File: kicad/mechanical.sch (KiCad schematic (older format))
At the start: 70 parts, among them J1 CLK_IN, J10 DAT_IN, J15 5V, J16 GND, J2 DAT_IN, J7 5V, J8 GND, J9 CLK_IN

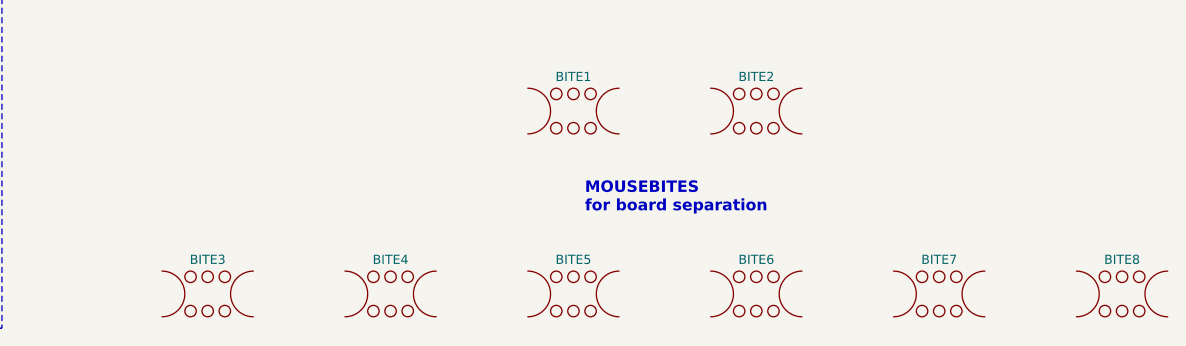
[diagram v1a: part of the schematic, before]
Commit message: KiCad v5 - new expansion headers, new qwiic headers, wider breakoff tabs
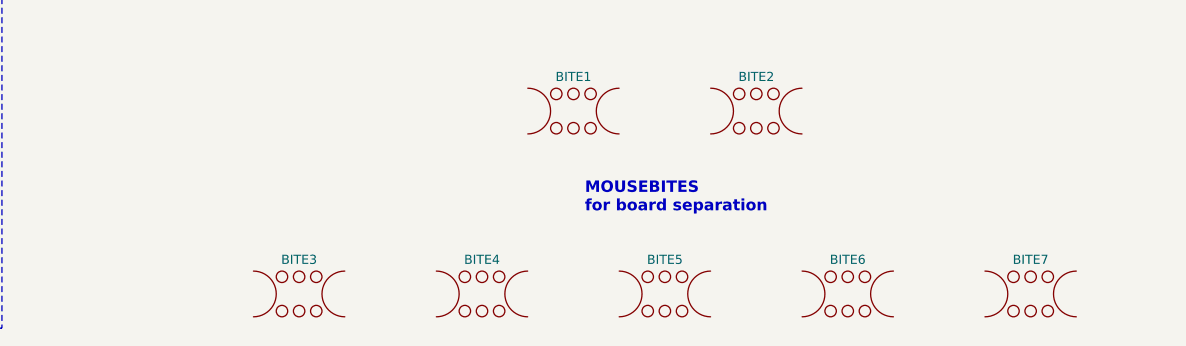
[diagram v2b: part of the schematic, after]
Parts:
- removed BITE8: Mouse_Bite, ClockIOT_libs:mouse-bite-2.54mm-slot_OSH, symbol ClockIOT:Mouse_Bite
- BITE1, BITE2, BITE3, BITE4, BITE5, BITE6, BITE7: footprint ClockIOT_libs:mouse-bite-2.54mm-slot_OSH -> ClockIOT_libs:mouse-bite-0.3in-slot_OSH
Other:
- moved on the sheet: BITE3, BITE4, BITE5, BITE6, BITE7
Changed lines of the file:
@@
 EESchema Schematic File Version 4
-LIBS:ClockIOT-cache
-EELAYER 26 0
+EELAYER 30 0
 EELAYER END
 $Descr A4 11693 8268
@@
 F 0 "BITE1" H 8100 5050 40  0000 C CNN
 F 1 "Mouse_Bite" H 8100 5025 30  0001 C CNN
-F 2 "ClockIOT_libs:mouse-bite-2.54mm-slot_OSH" H 8100 4900 60  0001 C CNN
+F 2 "ClockIOT_libs:mouse-bite-0.3in-slot_OSH" H 8100 4900 60  0001 C CNN
 F 3 "" H 8100 4900 60  0000 C CNN
 F 4 "mfr_pn" H 8100 4900 50  0001 C CNN "manf#"
@@
 F 0 "BITE2" H 8900 5050 40  0000 C CNN
 F 1 "Mouse_Bite" H 8900 5025 30  0001 C CNN
-F 2 "ClockIOT_libs:mouse-bite-2.54mm-slot_OSH" H 8900 4900 60  0001 C CNN
+F 2 "ClockIOT_libs:mouse-bite-0.3in-slot_OSH" H 8900 4900 60  0001 C CNN
 F 3 "" H 8900 4900 60  0000 C CNN
 F 4 "mfr_pn" H 8900 4900 50  0001 C CNN "manf#"
@@
 L ClockIOT:Mouse_Bite BITE5
 U 1 1 5A4A2BA0
-P 8100 5700
-F 0 "BITE5" H 8100 5850 40  0000 C CNN
-F 1 "Mouse_Bite" H 8100 5825 30  0001 C CNN
-F 2 "ClockIOT_libs:mouse-bite-2.54mm-slot_OSH" H 8100 5700 60  0001 C CNN
-F 3 "" H 8100 5700 60  0000 C CNN
-F 4 "mfr_pn" H 8100 5700 50  0001 C CNN "manf#"
-	1    8100 5700
+P 8500 5700
+F 0 "BITE5" H 8500 5850 40  0000 C CNN
+F 1 "Mouse_Bite" H 8500 5825 30  0001 C CNN
+F 2 "ClockIOT_libs:mouse-bite-0.3in-slot_OSH" H 8500 5700 60  0001 C CNN
+F 3 "" H 8500 5700 60  0000 C CNN
+F 4 "mfr_pn" H 8500 5700 50  0001 C CNN "manf#"
+	1    8500 5700
 	1    0    0    -1
 $EndComp
@@
 L ClockIOT:Mouse_Bite BITE6
 U 1 1 5A4A2BA6
-P 8900 5700
-F 0 "BITE6" H 8900 5850 40  0000 C CNN
-F 1 "Mouse_Bite" H 8900 5825 30  0001 C CNN
-F 2 "ClockIOT_libs:mouse-bite-2.54mm-slot_OSH" H 8900 5700 60  0001 C CNN
-F 3 "" H 8900 5700 60  0000 C CNN
-F 4 "mfr_pn" H 8900 5700 50  0001 C CNN "manf#"
-	1    8900 5700
+P 9300 5700
+F 0 "BITE6" H 9300 5850 40  0000 C CNN
+F 1 "Mouse_Bite" H 9300 5825 30  0001 C CNN
+F 2 "ClockIOT_libs:mouse-bite-0.3in-slot_OSH" H 9300 5700 60  0001 C CNN
+F 3 "" H 9300 5700 60  0000 C CNN
+F 4 "mfr_pn" H 9300 5700 50  0001 C CNN "manf#"
+	1    9300 5700
 	1    0    0    -1
 $EndComp
@@
 L ClockIOT:Mouse_Bite BITE7
 U 1 1 5A4A2F4F
-P 9700 5700
-F 0 "BITE7" H 9700 5850 40  0000 C CNN
-F 1 "Mouse_Bite" H 9700 5825 30  0001 C CNN
-F 2 "ClockIOT_libs:mouse-bite-2.54mm-slot_OSH" H 9700 5700 60  0001 C CNN
-F 3 "" H 9700 5700 60  0000 C CNN
-F 4 "mfr_pn" H 9700 5700 50  0001 C CNN "manf#"
-	1    9700 5700
-	1    0    0    -1
-$EndComp
-$Comp
-L ClockIOT:Mouse_Bite BITE8
-U 1 1 5A4A2F55
-P 10500 5700
-F 0 "BITE8" H 10500 5850 40  0000 C CNN
-F 1 "Mouse_Bite" H 10500 5825 30  0001 C CNN
-F 2 "ClockIOT_libs:mouse-bite-2.54mm-slot_OSH" H 10500 5700 60  0001 C CNN
-F 3 "" H 10500 5700 60  0000 C CNN
-F 4 "mfr_pn" H 10500 5700 50  0001 C CNN "manf#"
-	1    10500 5700
+P 10100 5700
+F 0 "BITE7" H 10100 5850 40  0000 C CNN
+F 1 "Mouse_Bite" H 10100 5825 30  0001 C CNN
+F 2 "ClockIOT_libs:mouse-bite-0.3in-slot_OSH" H 10100 5700 60  0001 C CNN
+F 3 "" H 10100 5700 60  0000 C CNN
+F 4 "mfr_pn" H 10100 5700 50  0001 C CNN "manf#"
+	1    10100 5700
 	1    0    0    -1
 $EndComp
@@
 L ClockIOT:Mouse_Bite BITE3
 U 1 1 5A4A335C
-P 6500 5700
-F 0 "BITE3" H 6500 5850 40  0000 C CNN
-F 1 "Mouse_Bite" H 6500 5825 30  0001 C CNN
-F 2 "ClockIOT_libs:mouse-bite-2.54mm-slot_OSH" H 6500 5700 60  0001 C CNN
-F 3 "" H 6500 5700 60  0000 C CNN
-F 4 "mfr_pn" H 6500 5700 50  0001 C CNN "manf#"
-	1    6500 5700
+P 6900 5700
+F 0 "BITE3" H 6900 5850 40  0000 C CNN
+F 1 "Mouse_Bite" H 6900 5825 30  0001 C CNN
+F 2 "ClockIOT_libs:mouse-bite-0.3in-slot_OSH" H 6900 5700 60  0001 C CNN
+F 3 "" H 6900 5700 60  0000 C CNN
+F 4 "mfr_pn" H 6900 5700 50  0001 C CNN "manf#"
+	1    6900 5700
 	1    0    0    -1
 $EndComp
@@
 L ClockIOT:Mouse_Bite BITE4
 U 1 1 5A4A3362
-P 7300 5700
-F 0 "BITE4" H 7300 5850 40  0000 C CNN
-F 1 "Mouse_Bite" H 7300 5825 30  0001 C CNN
-F 2 "ClockIOT_libs:mouse-bite-2.54mm-slot_OSH" H 7300 5700 60  0001 C CNN
-F 3 "" H 7300 5700 60  0000 C CNN
-F 4 "mfr_pn" H 7300 5700 50  0001 C CNN "manf#"
-	1    7300 5700
-	1    0    0    -1
-$EndComp
+P 7700 5700
+F 0 "BITE4" H 7700 5850 40  0000 C CNN
+F 1 "Mouse_Bite" H 7700 5825 30  0001 C CNN
+F 2 "ClockIOT_libs:mouse-bite-0.3in-slot_OSH" H 7700 5700 60  0001 C CNN
+F 3 "" H 7700 5700 60  0000 C CNN
+F 4 "mfr_pn" H 7700 5700 50  0001 C CNN "manf#"
+	1    7700 5700
+	1    0    0    -1
+$EndComp
